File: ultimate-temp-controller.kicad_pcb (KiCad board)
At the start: 2 copper layers, 80 x 100 mm, 63 parts, among them CON1 SD_Card, IC1 ATMEGA328-A, P1 ISP, P10 RS485, P2 BUTTONS, P3 OPEN_DRAIN, P4 POWER, P5 I2C1, P6 I2C2, P8 THERMOCOUPLE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

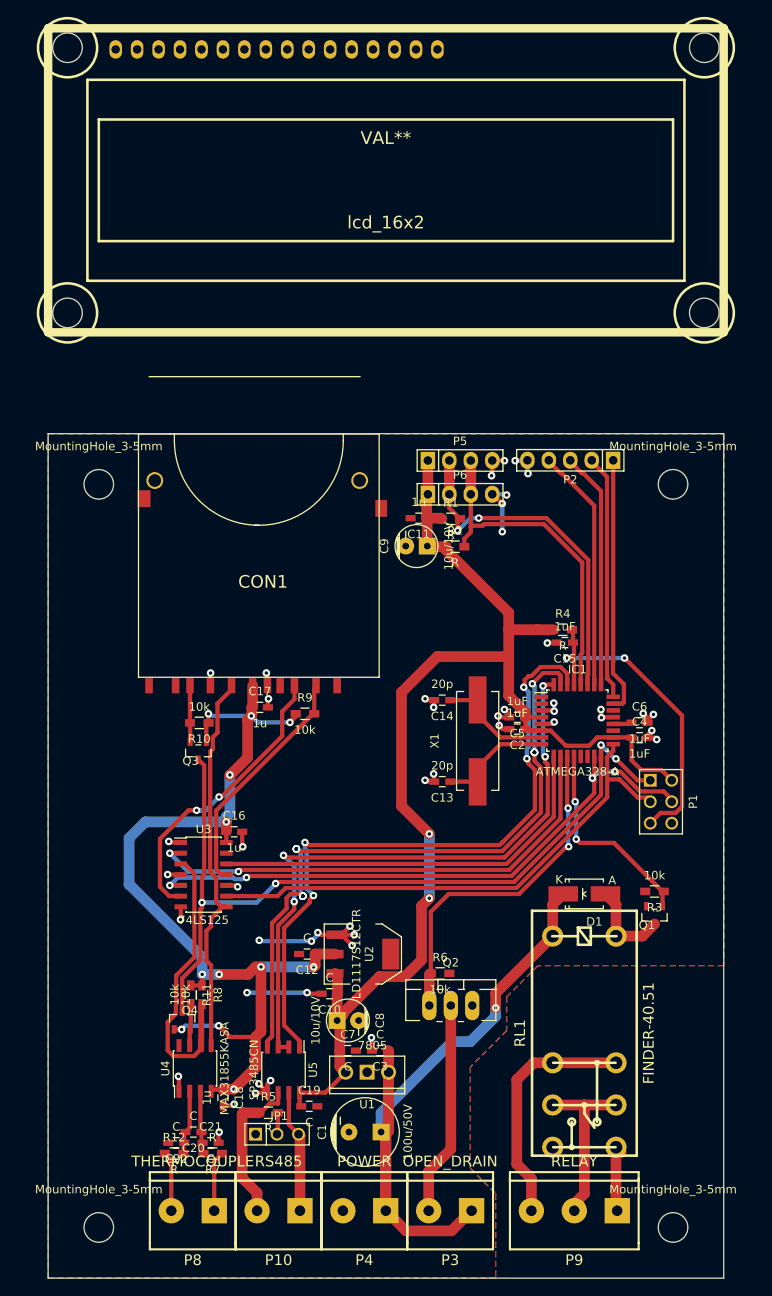
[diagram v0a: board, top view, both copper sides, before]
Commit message: Add dimensions
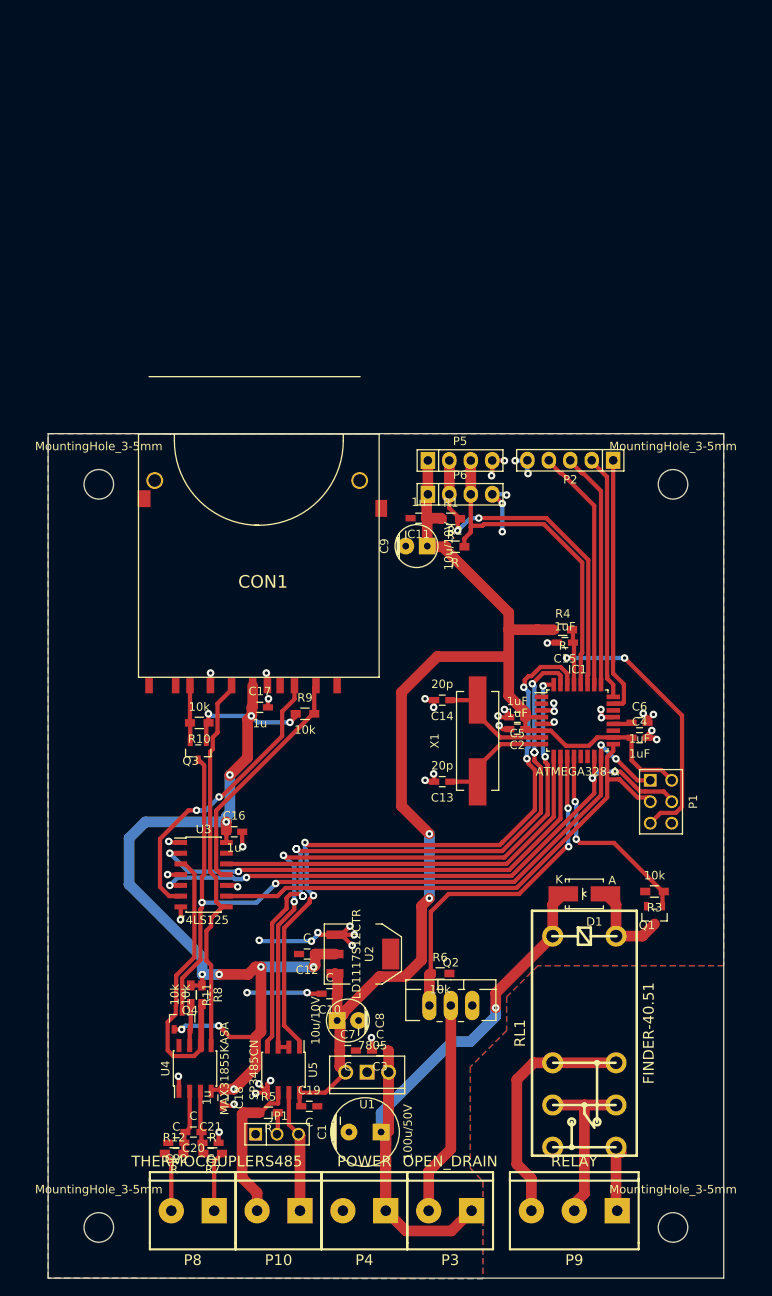
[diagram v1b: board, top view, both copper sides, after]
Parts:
- removed lcd_16x2: VAL**, w_indicators:lcd_16x2

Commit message: Put silkscreen to order
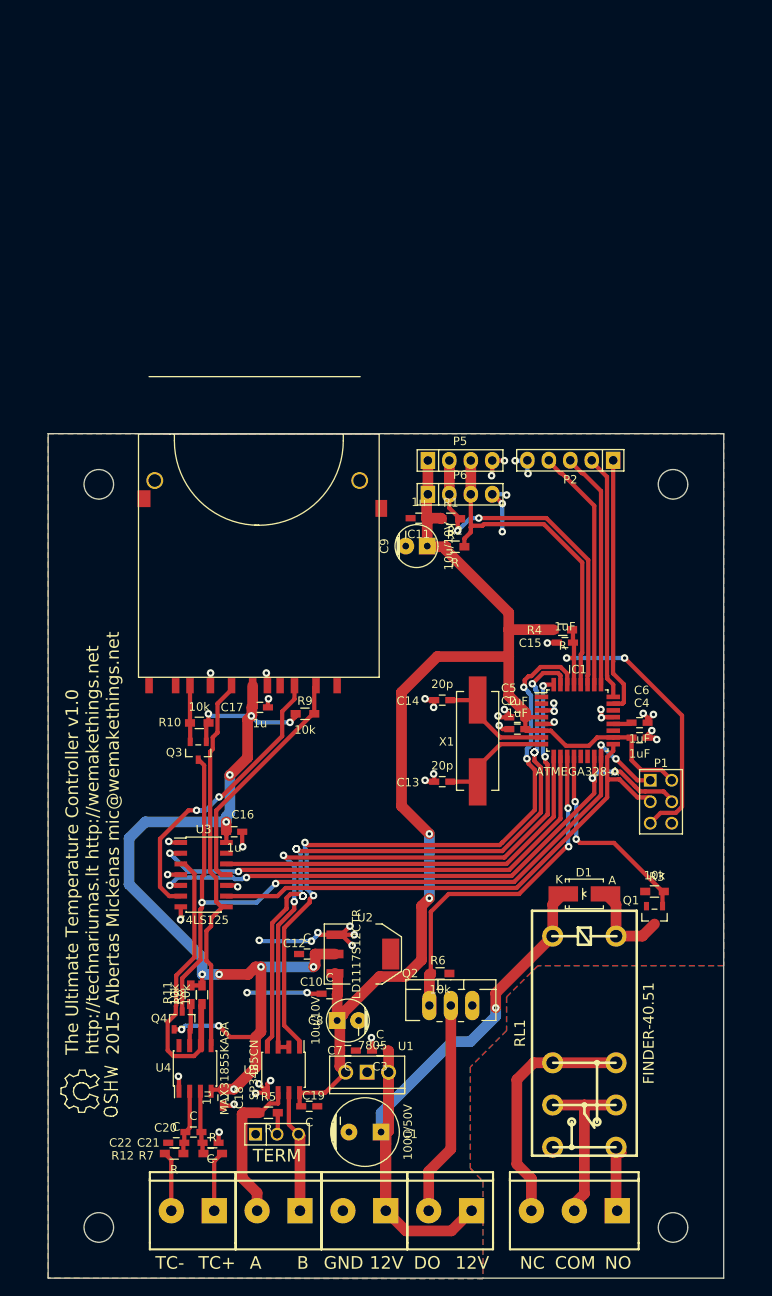
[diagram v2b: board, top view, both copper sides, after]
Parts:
- added Symbol_OSHW-Logo_SilkScreen: VAL**, Symbols:Symbol_OSHW-Logo_SilkScreen, F.Cu at (95.0, 166.9)
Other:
- board text added: "12V"
- board text added: "A"
- board text added: "B"
- board text added: "COM"
- board text added: "DO"
- board text added: "GND"
- board text added: "NC"
- board text added: "NO"
- board text added: "TC+"
- board text added: "TC-"
- board text added: "TERM"
- board text added: "The Ultimate Temperature Controller v1.0 http://technariumas.lt http://wemakethings.net 2015 Albertas Mickėnas mic@wemakethings.net"

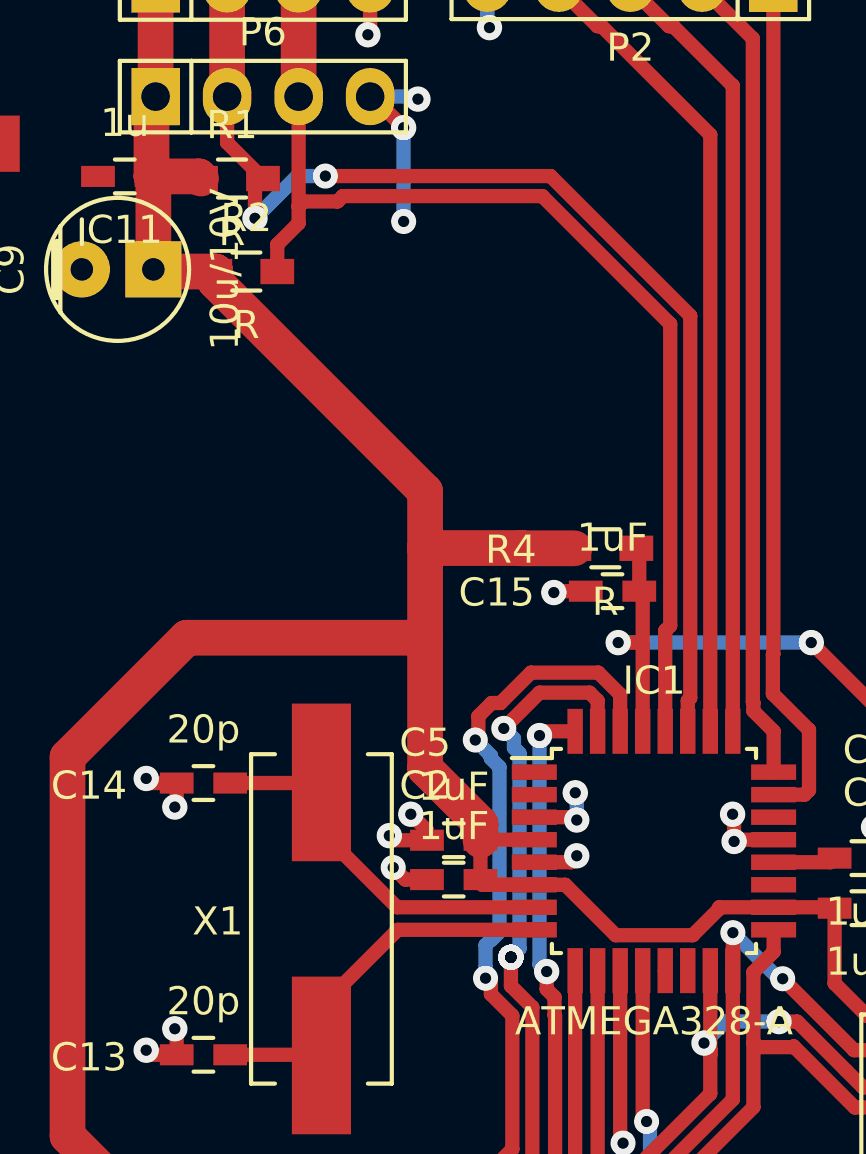
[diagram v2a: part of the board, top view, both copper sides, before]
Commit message: Add a serial header for Arduino compatible programming
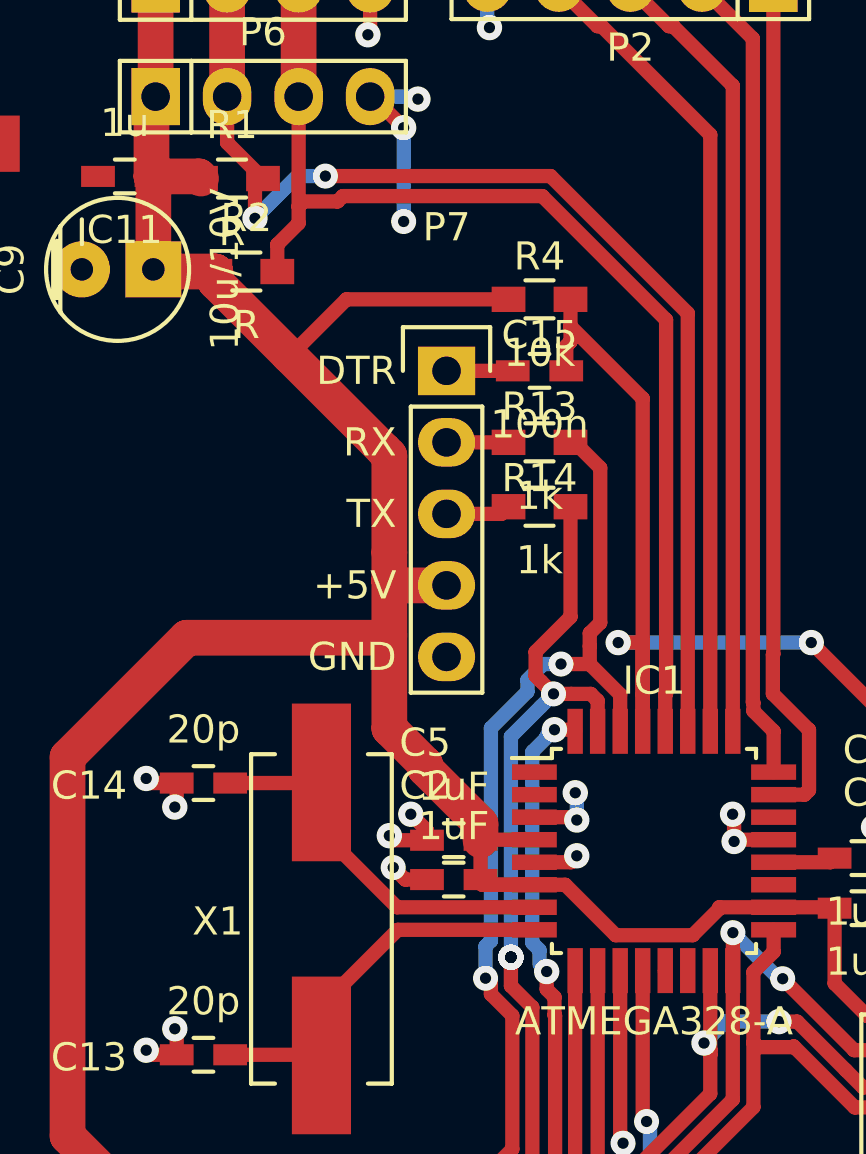
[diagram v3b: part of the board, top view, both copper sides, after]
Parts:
- added P7: CONN_01X05, Pin_Headers:Pin_Header_Straight_1x05, F.Cu at (146.3, 105.9)
- added R13: 1k, Resistors_SMD:R_0603_HandSoldering, F.Cu at (149.6, 108.5)
- added R14: 1k, Resistors_SMD:R_0603_HandSoldering, F.Cu at (149.6, 110.7)
- C15: value 1uF -> 100n
- R4: value R -> 10k
- moved R4 9.15 mm to (149.6, 103.4)
- moved C15 8.24 mm to (149.6, 105.9), turned to 0 degrees
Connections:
- C15 pad 1: /controller/RESET -> /controller/DTR
- C15 pad 2: GND -> /controller/RESET
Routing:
- net /controller/RESET: track 39.7 -> 54.0 mm
- net /controller/RXD: track 79.8 -> 87.6 mm
- net /controller/TXD: track 79.1 -> 85.7 mm
- net +5V: track 153.2 -> 157.4 mm
- net /controller/DTR: track 0.00 -> 2.35 mm
- net /controller/TX: track 0.00 -> 2.31 mm
- net /controller/RX: track 0.00 -> 2.20 mm
- net GND: track 81.8 -> 80.6 mm, vias 47 -> 46
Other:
- board text added: "+5V"
- board text added: "DTR"
- board text added: "RX"
- board text added: "TX"

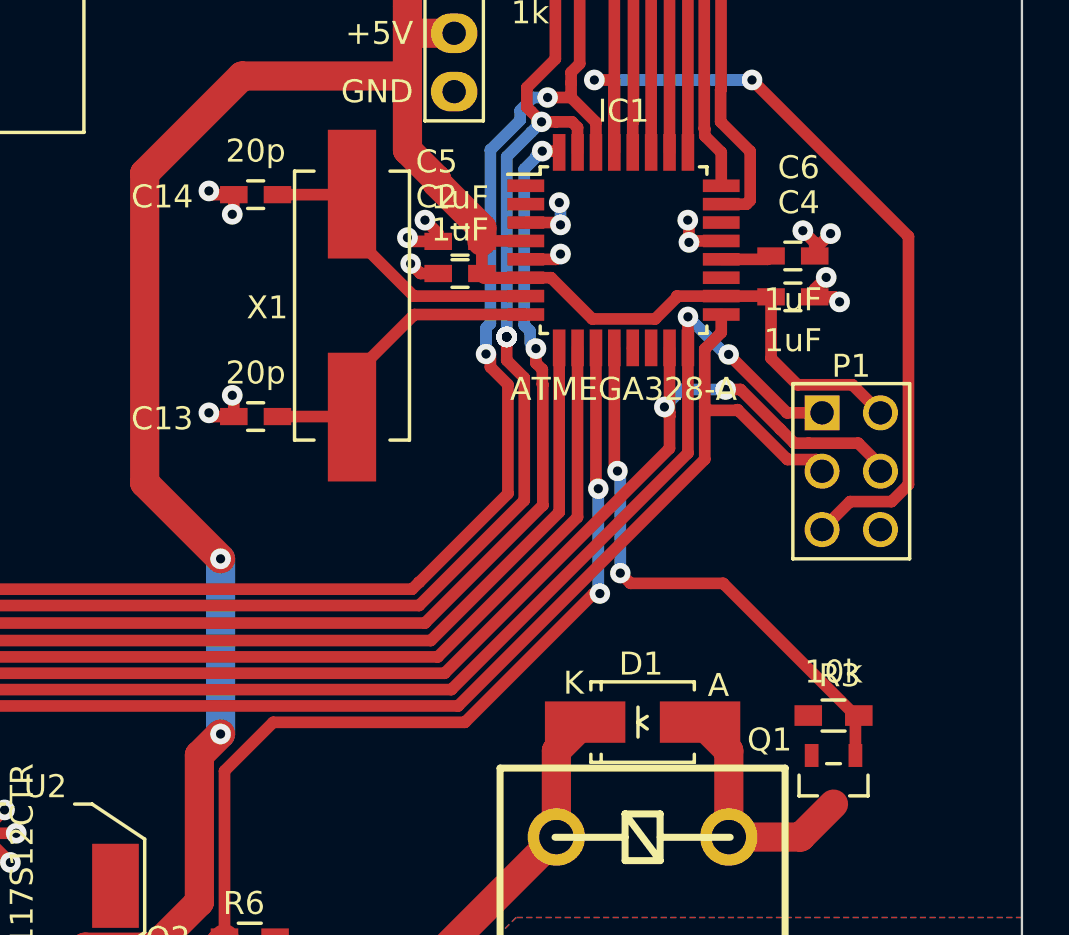
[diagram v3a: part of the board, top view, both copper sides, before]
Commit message: Break out leftover pins
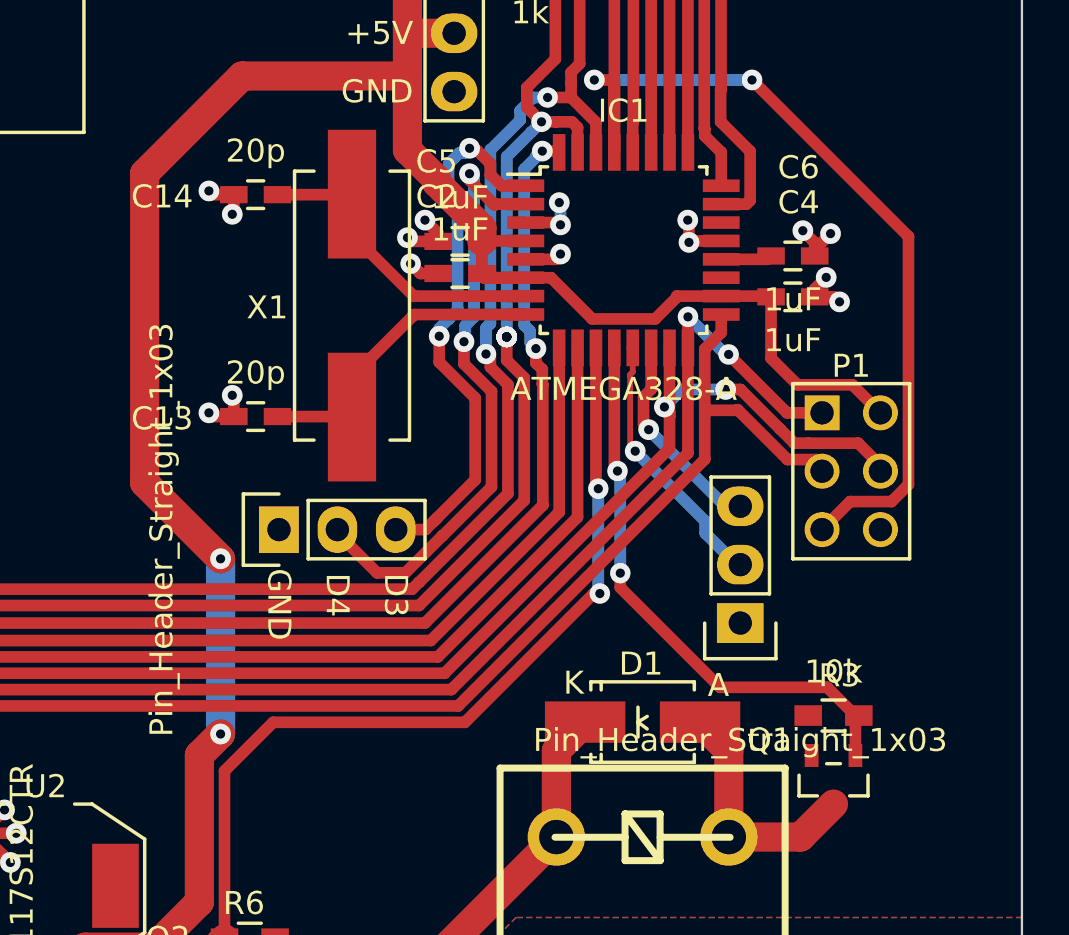
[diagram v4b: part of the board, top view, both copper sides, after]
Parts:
- added Pin_Header_Straight_1x03: VAL**, Pin_Headers:Pin_Header_Straight_1x03, F.Cu at (158.8, 139.2)
- added Pin_Header_Straight_1x03: VAL**, Pin_Headers:Pin_Header_Straight_1x03, F.Cu at (138.7, 135.1)
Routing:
- net Net-(IC1-Pad2): track 0.00 -> 26.8 mm, vias 0 -> 2
- net Net-(IC1-Pad1): track 0.00 -> 24.0 mm, vias 0 -> 2
- net Net-(IC1-Pad13): track 0.02 -> 11.6 mm, vias 0 -> 1
- net Net-(IC1-Pad14): track 0.00 -> 9.76 mm, vias 0 -> 1
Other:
- board text added: "D3"
- board text added: "D4"

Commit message: Add some silkscreen
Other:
- board text added: "D10"
- board text added: "D9"
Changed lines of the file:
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@@
     (area 90.949999 88.949999 171.050001 189.050001)
     (thickness 1.6)
-    (drawings 42)
+    (drawings 45)
     (tracks 815)
     (zones 0)
@@
     )
   )
+  (gr_text D10 (at 156.972 134.112) (layer F.SilkS)
+    (effects (font (size 1 1) (thickness 0.15)) (justify right))
+  )
+  (gr_text D9 (at 156.972 136.652) (layer F.SilkS)
+    (effects (font (size 1 1) (thickness 0.15)) (justify right))
+  )
+  (gr_text GND (at 156.972 139.192) (layer F.SilkS)
+    (effects (font (size 1 1) (thickness 0.15)) (justify right))
+  )
   (gr_text D3 (at 143.764 138.938 270) (layer F.SilkS)
